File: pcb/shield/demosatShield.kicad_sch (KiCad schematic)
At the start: 17 parts, among them J1 Power, J2 Digital/PWM, J3 Analog, J4 Digital/PWM, U1 SSCDANN150PGAA5

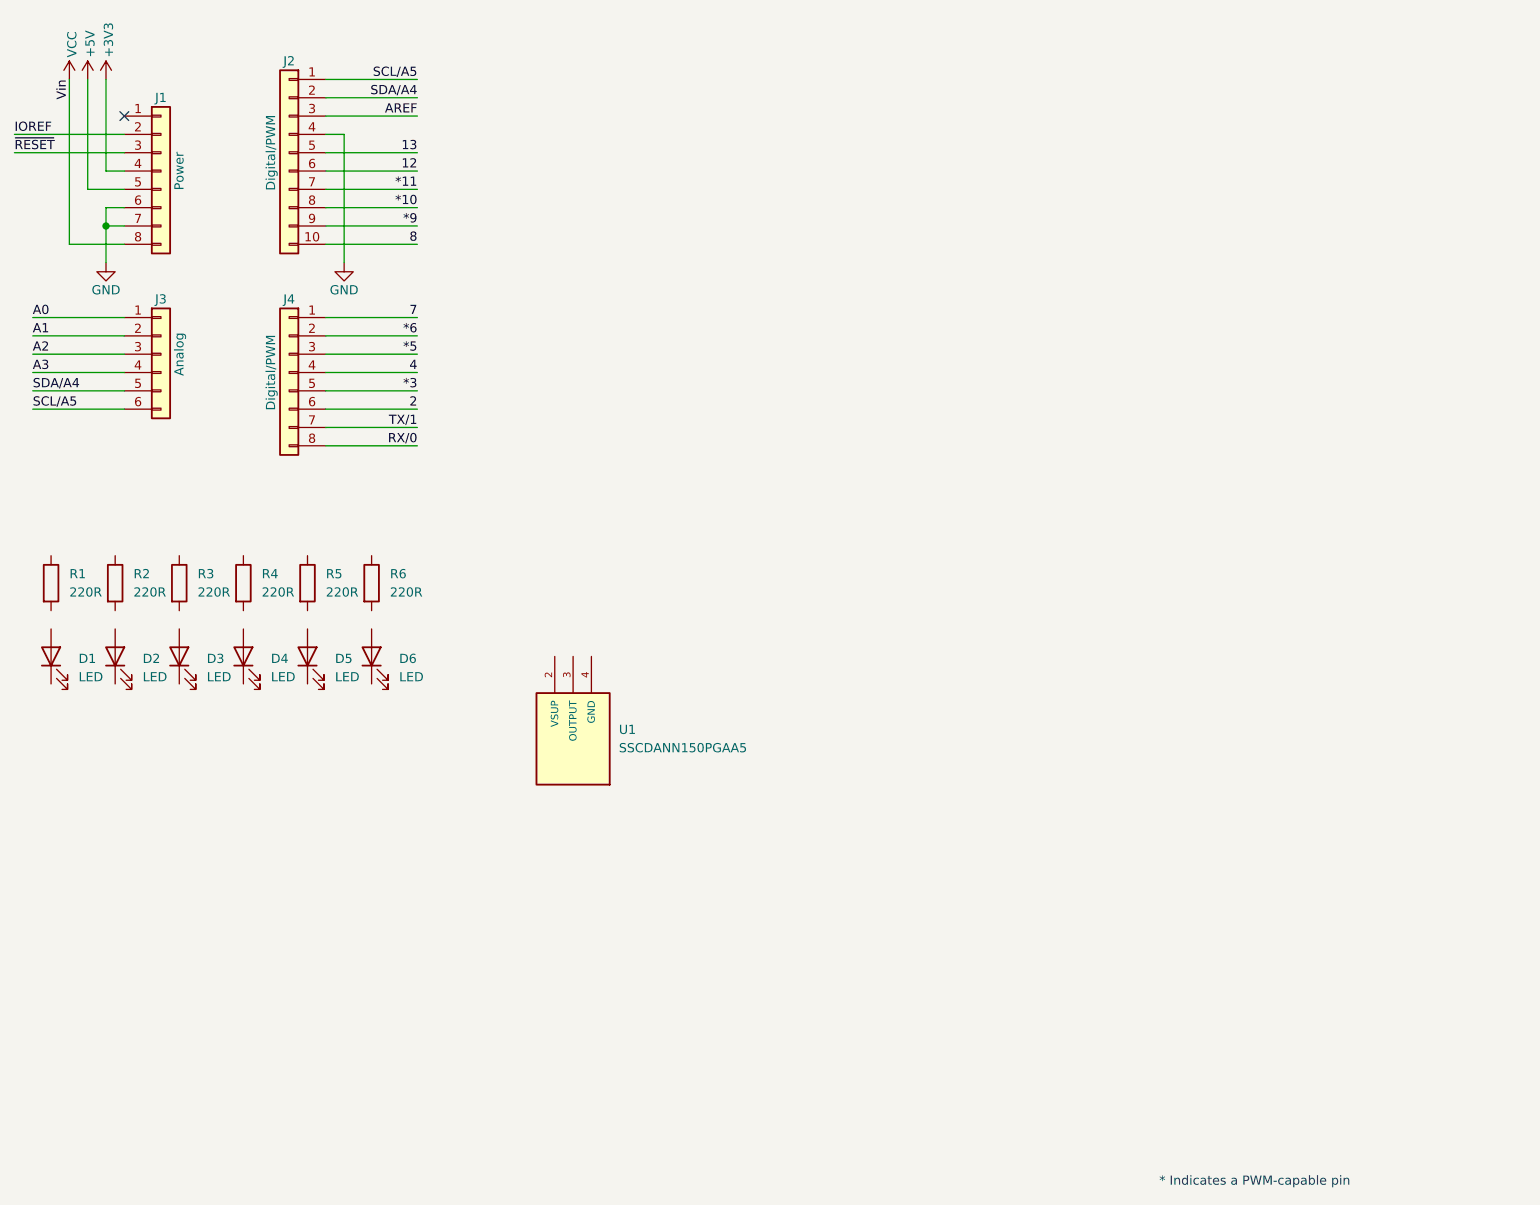
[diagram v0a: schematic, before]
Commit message: updated kicad project: schematic for sensors
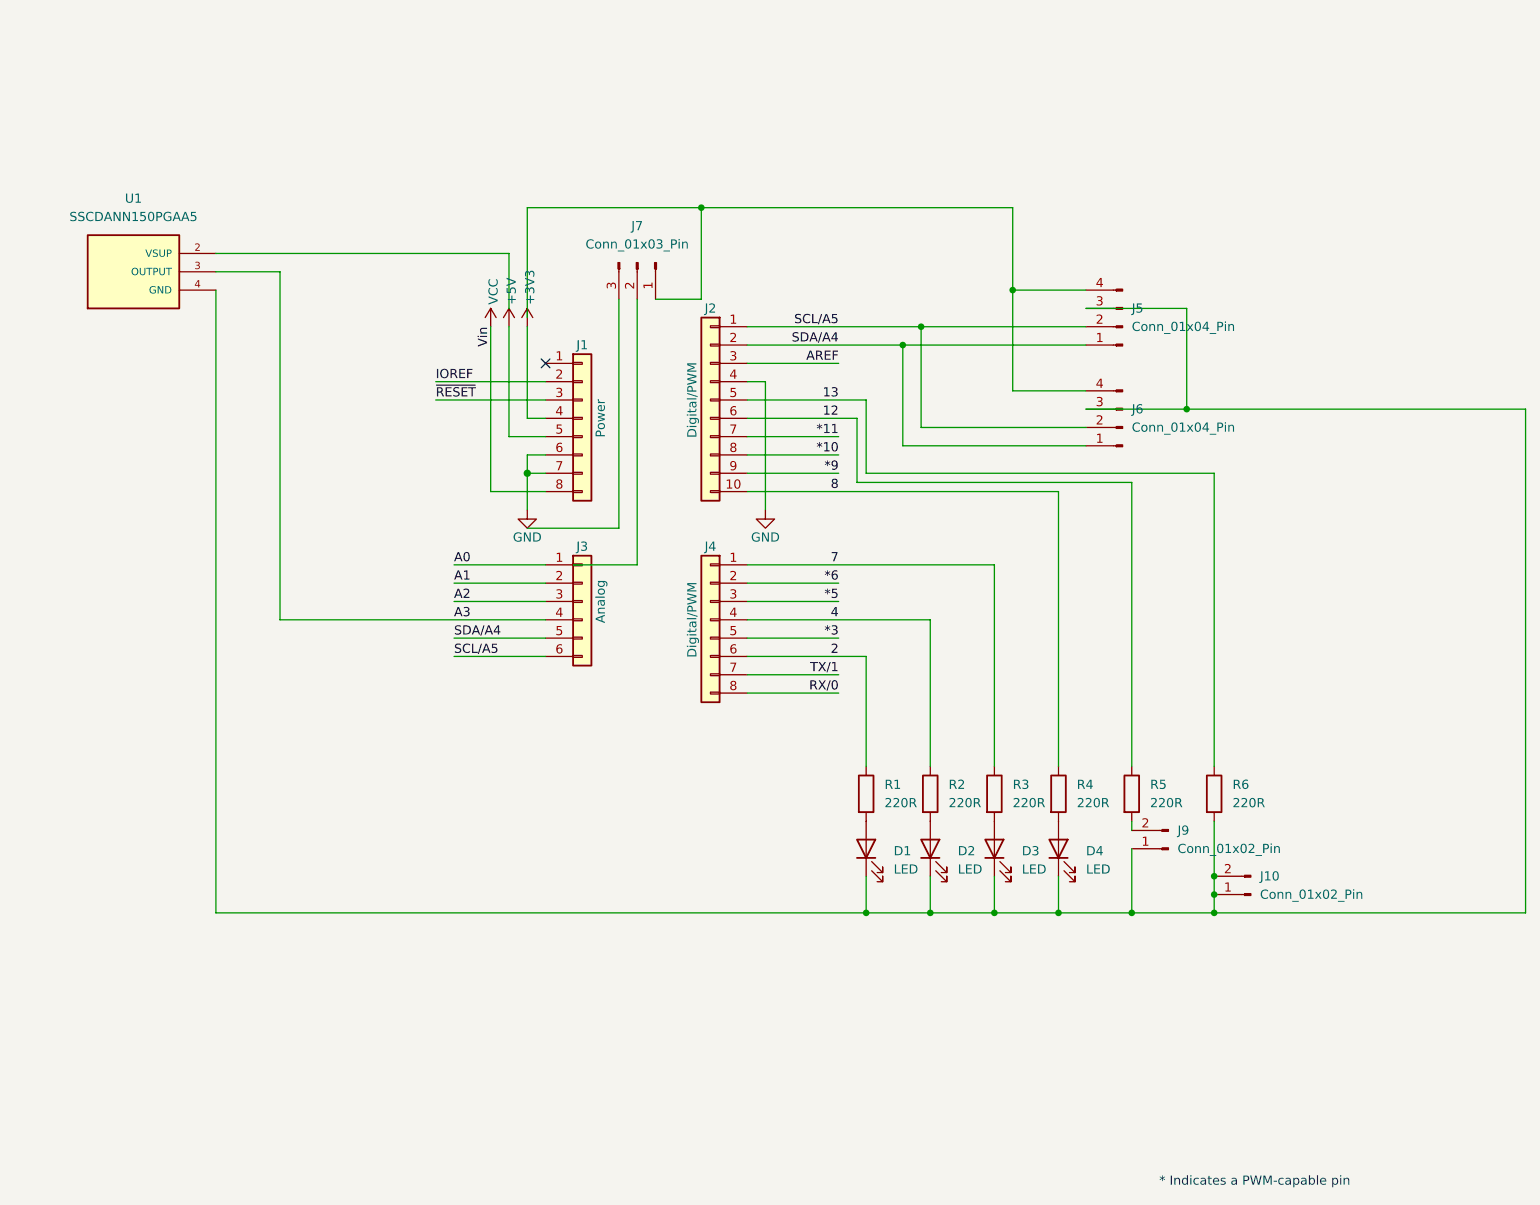
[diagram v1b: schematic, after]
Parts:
- removed D5, D6: LED, LED_THT:LED_D3.0mm_Horizontal_O3.81mm_Z10.0mm, symbol Device:LED
- added J10, J9: Conn_01x02_Pin, symbol Connector:Conn_01x02_Pin
- added J5, J6: Conn_01x04_Pin, Connector_JST:JST_PH_S4B-PH-SM4-TB_1x04-1MP_P2.00mm_Horizontal, symbol Connector:Conn_01x04_Pin
- added J7: Conn_01x03_Pin, symbol Connector:Conn_01x03_Pin
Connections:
- net 12: now also R5.1
- net 13: now also R6.1
- net 2: now also R1.1
- net 4: now also R2.1
- net 7: now also R3.1
- net 8: now also R4.1
- net A3: now also U1.3 (OUTPUT)
- net SCL/A5: now also J5.2 (Pin_2), J6.2 (Pin_2)
- net SDA/A4: now also J5.1 (Pin_1), J6.1 (Pin_1)
- net at R5.2: now also J9.2 (Pin_2)
- net at R3.2: now also D3.2 (A)
- net at R4.2: now also D4.2 (A)
- net at D1.1 (K): now also D2.1 (K), D3.1 (K), D4.1 (K), R6.2, U1.4 (GND), J10.1 (Pin_1), J10.2 (Pin_2), J5.3 (Pin_3), J6.3 (Pin_3), J9.1 (Pin_1)
- net at D1.2 (A): now also R1.2
- net at D2.2 (A): now also R2.2
- new net: J5.4 (Pin_4), J6.4 (Pin_4), J7.1 (Pin_1)
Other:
- moved on the sheet: D1, D2, D3, D4, J1, J2, J3, J4, R1, R2, R3, R4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

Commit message: kicad: cleaned up, moved all leds to the lower digital header, added socket for openlog
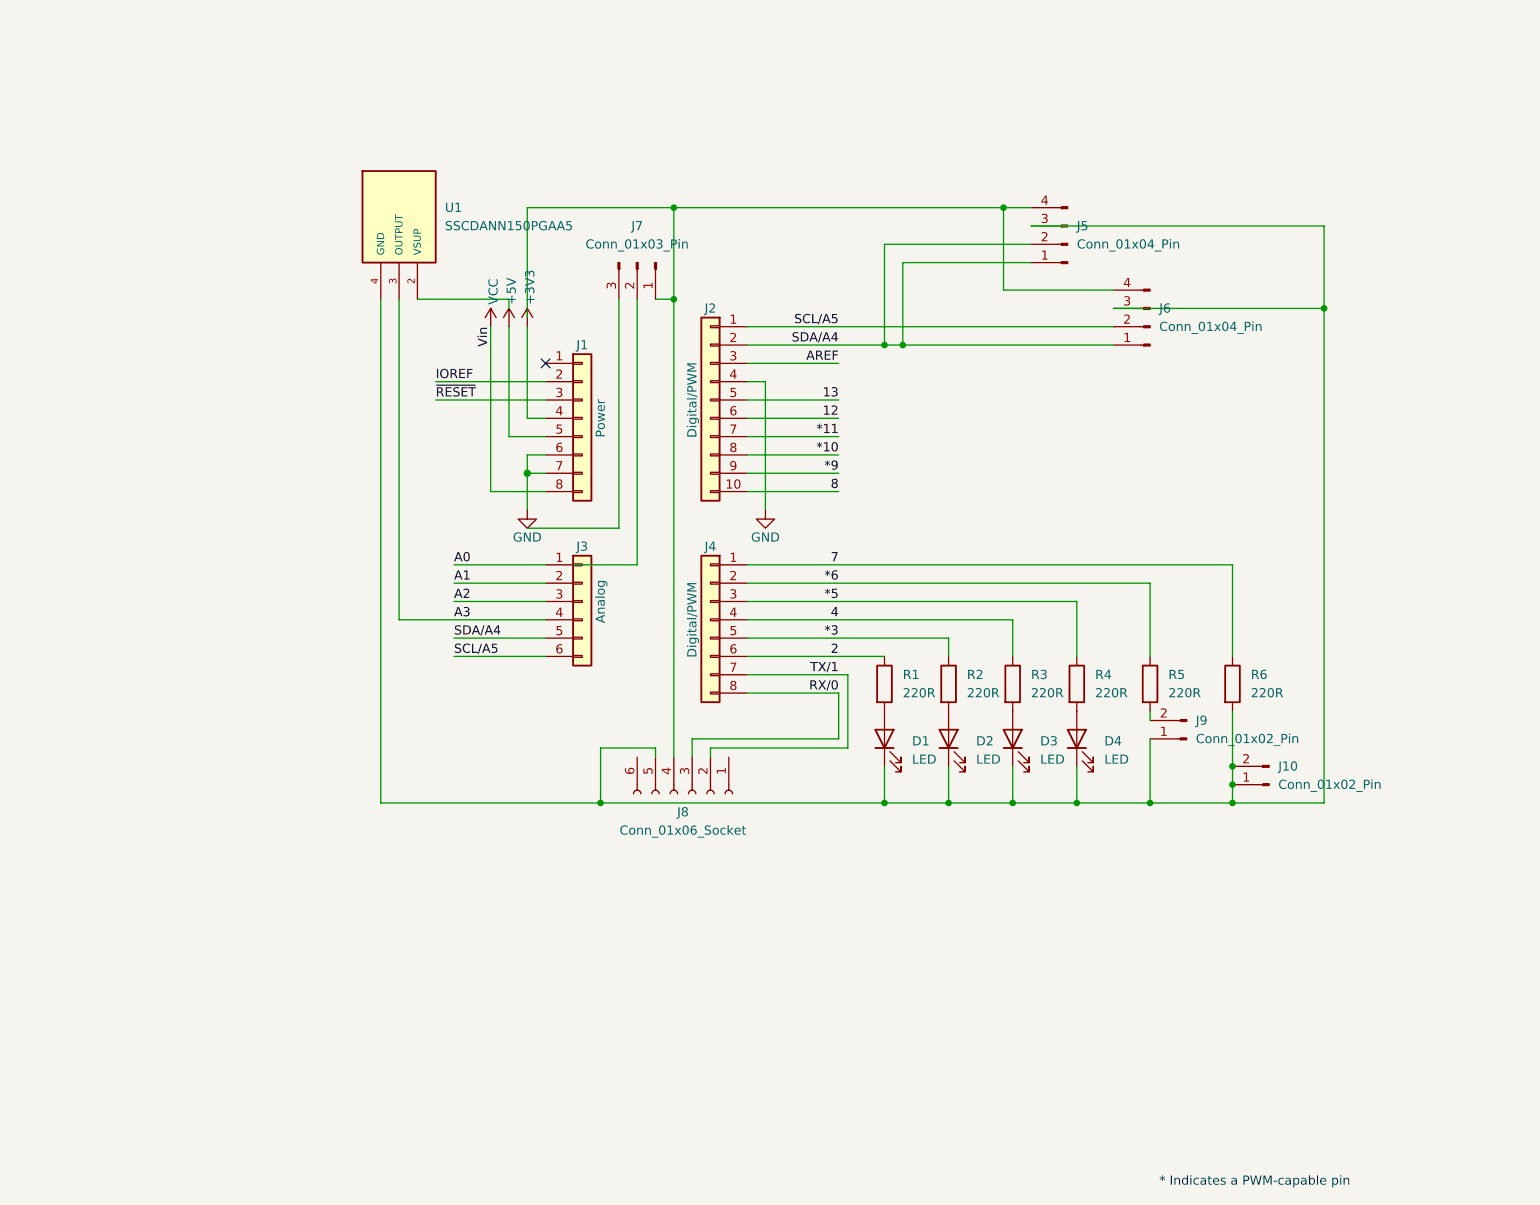
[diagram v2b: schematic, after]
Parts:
- added J8: Conn_01x06_Socket, symbol Connector:Conn_01x06_Socket
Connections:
- net *3: now also R2.1
- net *5: now also R4.1
- net *6: now also R5.1
- net 12: no longer R5.1
- net 13: no longer R6.1
- net 4: now also R3.1; no longer R2.1
- net 7: now also R6.1; no longer R3.1
- net 8: no longer R4.1
- net RX/0: now also J8.3 (Pin_3)
- net SCL/A5: no longer J5.2 (Pin_2)
- net SDA/A4: now also J5.2 (Pin_2)
- net TX/1: now also J8.2 (Pin_2)
- net at D1.1 (K), D2.1 (K), D3.1 (K)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: now also J8.5 (Pin_5)
- net at J5.4 (Pin_4), J6.4 (Pin_4), J7.1 (Pin_1): now also J8.4 (Pin_4)
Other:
- moved on the sheet: D1, D2, D3, D4, J10, J5, J6, J9, R1, R2, R3, R4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
